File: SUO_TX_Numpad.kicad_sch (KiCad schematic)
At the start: 17 parts, among them J1 USB_C_Receptacle_USB2.0_16P, SW1 BOOT, U1 STM32F411CEUx, U2 XC6206PxxxMR-Regulator_Linear, U3 USBLC6-2SC6, Y1 XTAL OSC XO 8.0000MHZ HCMOS S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

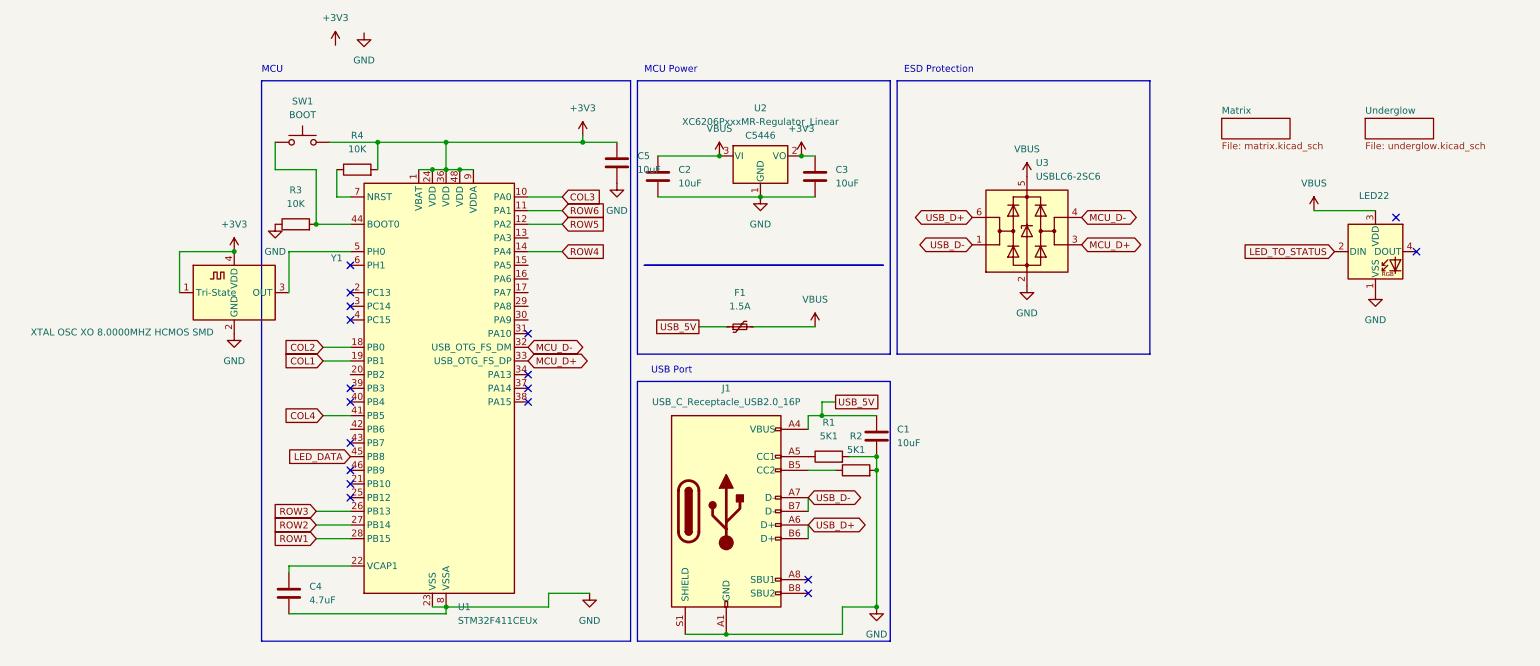
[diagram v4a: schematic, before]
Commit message: Pulled A10 to ground; found that a BlackPill dev board wo'nt DFU properly without it. Updated SK6812MINI-E footprint to be a rotated one; track layout stays the same, but the old footprint was incorrect, resulting in all key LEDs shorting out
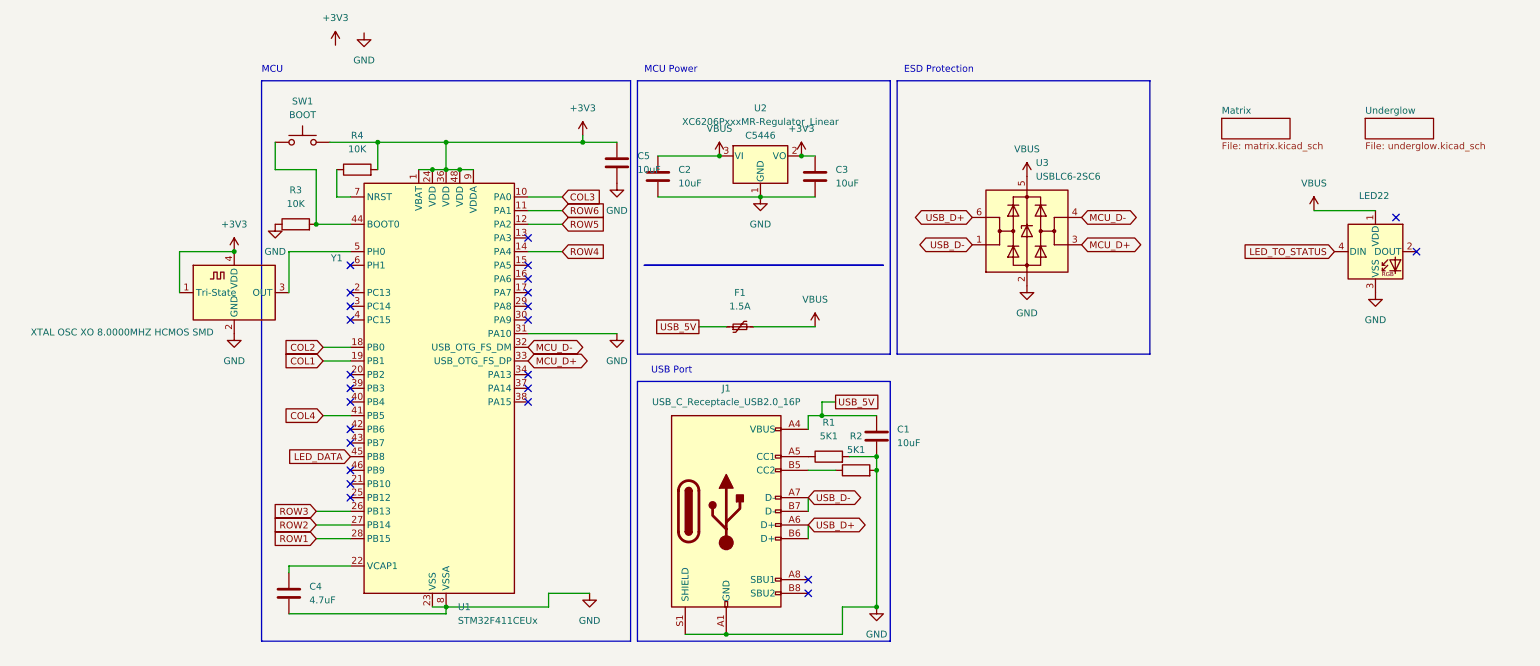
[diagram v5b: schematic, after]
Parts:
- LED22: footprint kicad-keyboard-parts:MX_SK6812MINI-E_REV -> kicad-keyboard-parts:MX_SK6812MINI-E_REV_ROTATED; symbol LED:SK6812MINI-E -> kicad-keyboard-parts:SK6812MINI-E
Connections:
- net GND: now also LED22.3 (VSS), U1.31 (PA10); no longer LED22.1 (VSS)
- net LED_TO_STATUS: now also LED22.4 (DIN); no longer LED22.2 (DIN)
- net VBUS: now also LED22.1 (VDD); no longer LED22.3 (VDD)
- no-connect marks 18 -> 25
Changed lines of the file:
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@@
 	)
 	(no_connect
-		(at 78.74 72.39)
-	)
-	(no_connect
 		(at 45.72 100.33)
 	)
@@
 	)
 	(no_connect
+		(at 78.74 67.31)
+	)
+	(no_connect
 		(at 45.72 82.55)
 	)
@@
 	)
 	(no_connect
+		(at 78.74 59.69)
+	)
+	(no_connect
+		(at 45.72 90.17)
+	)
+	(no_connect
 		(at 45.72 67.31)
 	)
@@
 	)
 	(no_connect
+		(at 78.74 69.85)
+	)
+	(no_connect
 		(at 130.81 118.11)
 	)
 	(no_connect
+		(at 45.72 80.01)
+	)
+	(no_connect
+		(at 78.74 62.23)
+	)
+	(no_connect
 		(at 78.74 82.55)
 	)
 	(no_connect
+		(at 78.74 64.77)
+	)
+	(no_connect
+		(at 78.74 54.61)
+	)
+	(no_connect
 		(at 45.72 85.09)
 	)
@@
 	(wire
 		(pts
+			(xy 78.74 72.39) (xy 95.25 72.39)
+		)
+		(stroke
+			(width 0)
+			(type default)
+		)
+	)
+	(wire
+		(pts
 			(xy 130.81 107.95) (xy 130.81 110.49)
 		)
@@
 	)
 	(symbol
-		(lib_id "LED:SK6812MINI-E")
+		(lib_id "kicad-keyboard-parts:SK6812MINI-E")
 		(at 236.22 57.15 0)
 		(unit 1)
@@
 			)
 		)
-		(property "Footprint" "kicad-keyboard-parts:MX_SK6812MINI-E_REV"
+		(property "Footprint" "kicad-keyboard-parts:MX_SK6812MINI-E_REV_ROTATED"
 			(at 237.49 64.77 0)
 			(effects
@@
 					(unit 1)
 				)
+			)
+		)
+	)
+	(symbol
+		(lib_id "power:GND")
+		(at 95.25 72.39 0)
+		(unit 1)
+		(exclude_from_sim no)
+		(in_bom yes)
+		(on_board yes)
+		(dnp no)
+		(fields_autoplaced yes)
+		(property "Reference" "#PWR037"
+			(at 95.25 78.74 0)
+			(effects
+				(font
+					(size 1.27 1.27)
+				)
+				(hide yes)
+			)
+		)
+		(property "Value" "GND"
+			(at 95.25 77.47 0)
+			(effects
+				(font
+					(size 1.27 1.27)
+				)
+			)
+		)
+		(property "Footprint" ""
+			(at 95.25 72.39 0)
+			(effects
+				(font
+					(size 1.27 1.27)
+				)
+				(hide yes)
+			)
+		)
+		(property "Datasheet" ""
+			(at 95.25 72.39 0)
+			(effects
+				(font
+					(size 1.27 1.27)
+				)
+				(hide yes)
+			)
+		)
+		(property "Description" ""
+			(at 95.25 72.39 0)
+			(effects
+				(font
+					(size 1.27 1.27)
+				)
+			)
+		)
+		(pin "1"
+		)
+		(instances
+			(project "SUO_TX_Numpad"
+				(path "/4f42914a-d4c6-4461-b1c3-be7726ab46dc"
+					(reference "#PWR037")
+					(unit 1)
+				)

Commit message: Added 3225 active oscillator, unsure if pin 1 is in fact enable, is in fact active high, so a jumper pad to pick either is added
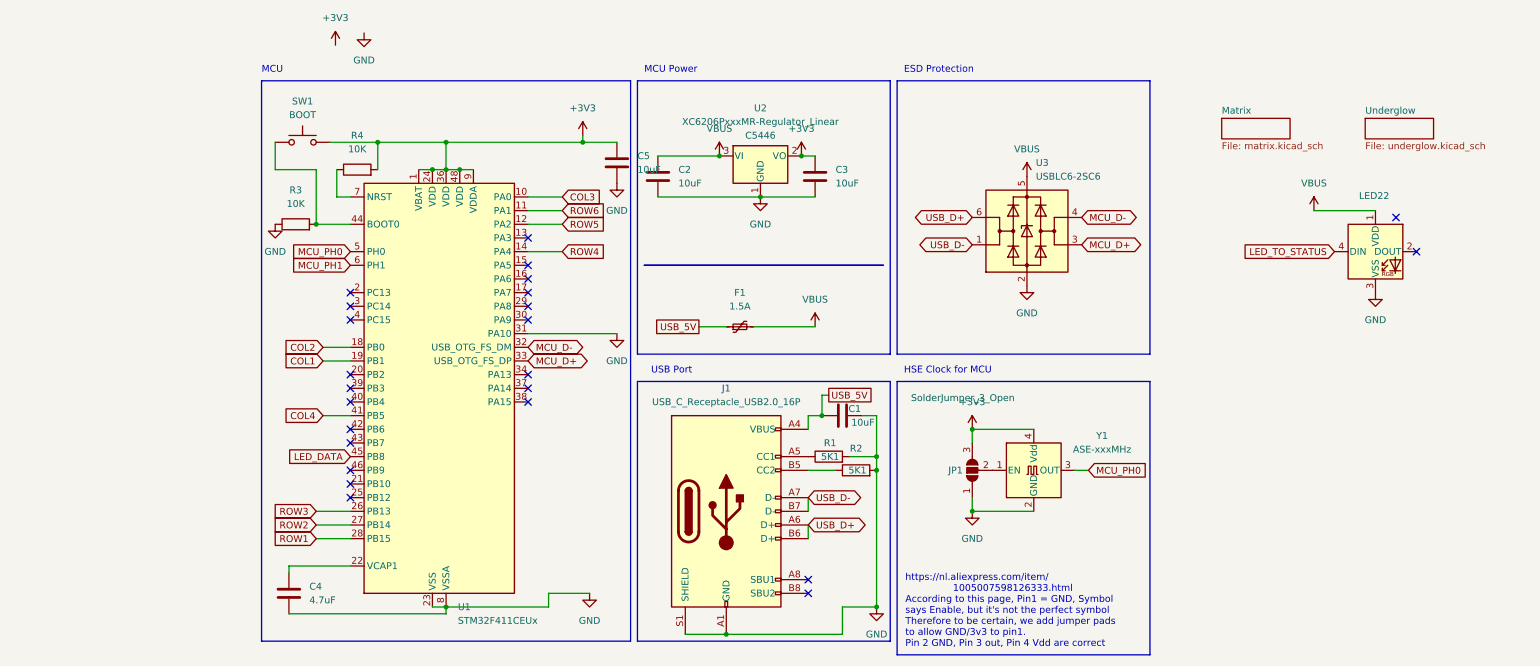
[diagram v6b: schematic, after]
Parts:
- removed Y1: XTAL OSC XO 8.0000MHZ HCMOS SMD, Oscillator:Oscillator_SMD_ECS_2520MV-xxx-xx-4Pin_2.5x2.0mm, symbol Oscillator:ECS-2520MV-xxx-xx
- added JP1: SolderJumper_3_Open, Jumper:SolderJumper-3_P1.3mm_Open_RoundedPad1.0x1.5mm, symbol Jumper:SolderJumper_3_Open
- added Y1: ASE-xxxMHz, Oscillator:Oscillator_SMD_Abracon_ASE-4Pin_3.2x2.5mm, symbol Oscillator:ASE-xxxMHz
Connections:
- net +3V3: now also JP1.3 (B), Y1.4 (Vdd)
- net GND: now also JP1.1 (A), Y1.2 (GND)
- net MCU_PH0: now reaches U1.5 (PH0)
- net MCU_PH0: now also Y1.3 (OUT)
- net MCU_PH1: now reaches U1.6 (PH1)
- new net: JP1.2 (C), Y1.1 (EN)
- no-connect marks 25 -> 24
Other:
- note added: "HSE Clock for MCU"
- note added: "https://nl.aliexpress.com/item/ 1005007598126333.html According to this page, Pin1 = GND, Symbol says Enable, but it's not the perfect symbol Therefore to be certain, we add jumper pads to allow GND/3v3 to pin1. Pin 2 GND, Pin 3 out, Pin 4 Vdd are correct"
- moved on the sheet: C1

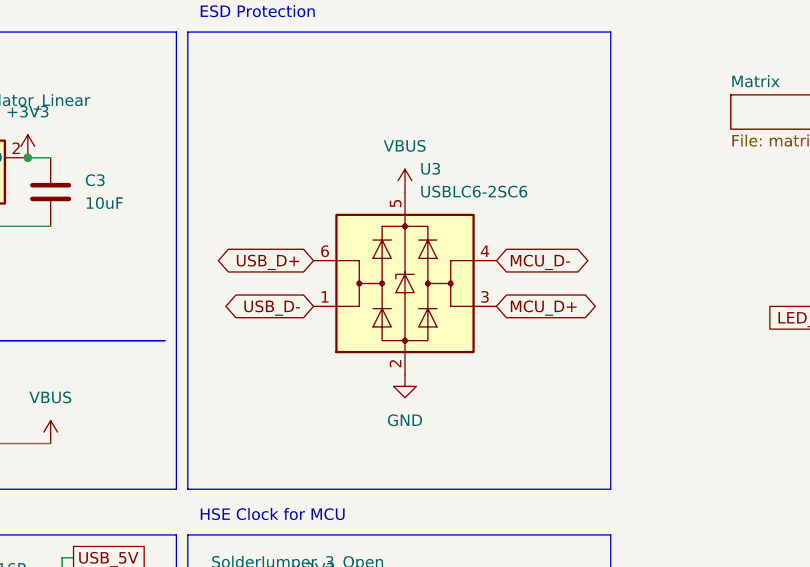
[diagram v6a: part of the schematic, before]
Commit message: Fixed wiring mistake on USBLC6-2SC6
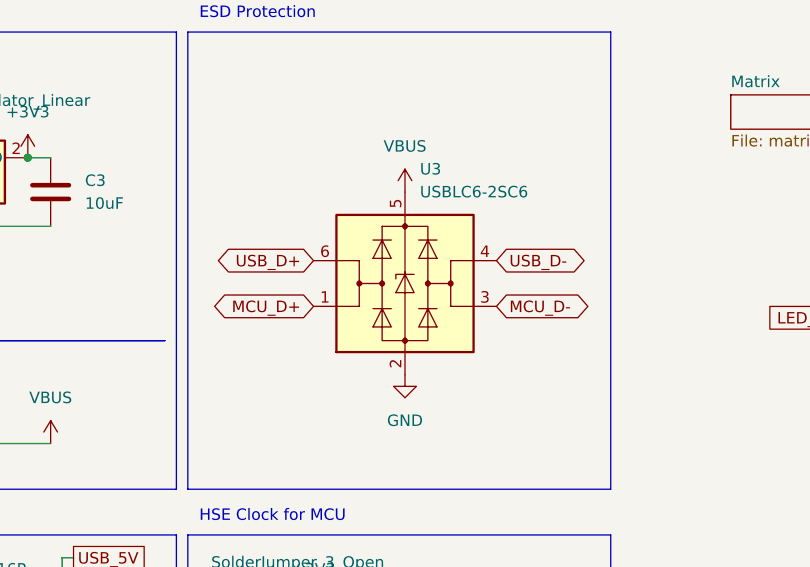
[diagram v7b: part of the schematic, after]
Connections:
- net MCU_D+: now also U3.1 (I/O1); no longer U3.3 (I/O2)
- net MCU_D-: now also U3.3 (I/O2); no longer U3.4 (I/O2)
- net USB_D-: now also U3.4 (I/O2); no longer U3.1 (I/O1)
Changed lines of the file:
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@@
+		)
+	)
+	(global_label "ROW4"
+		(shape input)
+		(at 85.09 57.15 0)
+		(fields_autoplaced yes)
+		(effects
+			(font
+				(size 1.27 1.27)
+			)
+			(justify left)
+		)
+		(property "Intersheetrefs" "${INTERSHEET_REFS}"
+			(at 93.3366 57.15 0)
+			(effects
+				(font
+					(size 1.27 1.27)
+				)
+				(justify left)
+				(hide yes)
+			)
+		)
+	)
+	(global_label "COL1"
+		(shape input)
+		(at 40.64 77.47 180)
+		(fields_autoplaced yes)
+		(effects
+			(font
+				(size 1.27 1.27)
+			)
+			(justify right)
+		)
+		(property "Intersheetrefs" "${INTERSHEET_REFS}"
+			(at 32.8167 77.47 0)
+			(effects
+				(font
+					(size 1.27 1.27)
+				)
+				(justify right)
+				(hide yes)
+			)
+		)
+	)
+	(global_label "USB_D-"
+		(shape bidirectional)
+		(at 130.81 102.87 0)
+		(fields_autoplaced yes)
+		(effects
+			(font
+				(size 1.27 1.27)
+			)
+			(justify left)
+		)
+		(property "Intersheetrefs" "${INTERSHEET_REFS}"
+			(at 142.5265 102.87 0)
+			(effects
+				(font
+					(size 1.27 1.27)
+				)
+				(justify left)
+				(hide yes)
+			)
 		)
 	)
 	(global_label "MCU_D-"
 		(shape bidirectional)
-		(at 181.61 50.8 0)
-		(fields_autoplaced yes)
-		(effects
-			(font
-				(size 1.27 1.27)
-			)
-			(justify left)
-		)
-		(property "Intersheetrefs" "${INTERSHEET_REFS}"
-			(at 193.5684 50.8 0)
-			(effects
-				(font
-					(size 1.27 1.27)
-				)
-				(justify left)
+		(at 181.61 55.88 0)
+		(fields_autoplaced yes)
+		(effects
+			(font
+				(size 1.27 1.27)
+			)
+			(justify left)
+		)
+		(property "Intersheetrefs" "${INTERSHEET_REFS}"
+			(at 193.5684 55.88 0)
+			(effects
+				(font
+					(size 1.27 1.27)
+				)
+				(justify left)
+				(hide yes)
+			)
+		)
+	)
+	(global_label "MCU_PH0"
+		(shape input)
+		(at 45.72 57.15 180)
+		(fields_autoplaced yes)
+		(effects
+			(font
+				(size 1.27 1.27)
+			)
+			(justify right)
+		)
+		(property "Intersheetrefs" "${INTERSHEET_REFS}"
+			(at 33.9053 57.15 0)
+			(effects
+				(font
+					(size 1.27 1.27)
+				)
+				(justify right)
+				(hide yes)
+			)
+		)
+	)
+	(global_label "ROW3"
+		(shape input)
+		(at 39.37 105.41 180)
+		(fields_autoplaced yes)
+		(effects
+			(font
+				(size 1.27 1.27)
+			)
+			(justify right)
+		)
+		(property "Intersheetrefs" "${INTERSHEET_REFS}"
+			(at 31.1234 105.41 0)
+			(effects
+				(font
+					(size 1.27 1.27)
+				)
+				(justify right)
+				(hide yes)
+			)
+		)
+	)
+	(global_label "MCU_PH1"
+		(shape input)
+		(at 45.72 59.69 180)
+		(fields_autoplaced yes)
+		(effects
+			(font
+				(size 1.27 1.27)
+			)
+			(justify right)
+		)
+		(property "Intersheetrefs" "${INTERSHEET_REFS}"
+			(at 33.9053 59.69 0)
+			(effects
+				(font
+					(size 1.27 1.27)
+				)
+				(justify right)
 				(hide yes)
 			)
@@
 		)
 	)
-	(global_label "ROW4"
-		(shape input)
-		(at 85.09 57.15 0)
-		(fields_autoplaced yes)
-		(effects
-			(font
-				(size 1.27 1.27)
-			)
-			(justify left)
-		)
-		(property "Intersheetrefs" "${INTERSHEET_REFS}"
-			(at 93.3366 57.15 0)
-			(effects
-				(font
-					(size 1.27 1.27)
-				)
-				(justify left)
-				(hide yes)
-			)
-		)
-	)
-	(global_label "COL1"
-		(shape input)
-		(at 40.64 77.47 180)
-		(fields_autoplaced yes)
-		(effects
-			(font
-				(size 1.27 1.27)
-			)
-			(justify right)
-		)
-		(property "Intersheetrefs" "${INTERSHEET_REFS}"
-			(at 32.8167 77.47 0)
-			(effects
-				(font
-					(size 1.27 1.27)
-				)
-				(justify right)
-				(hide yes)
-			)
-		)
-	)
-	(global_label "USB_D-"
-		(shape bidirectional)
-		(at 130.81 102.87 0)
-		(fields_autoplaced yes)
-		(effects
-			(font
-				(size 1.27 1.27)
-			)
-			(justify left)
-		)
-		(property "Intersheetrefs" "${INTERSHEET_REFS}"
-			(at 142.5265 102.87 0)
-			(effects
-				(font
-					(size 1.27 1.27)
-				)
-				(justify left)
-				(hide yes)
-			)
-		)
-	)
-	(global_label "USB_D-"
+	(global_label "ROW2"
+		(shape input)
+		(at 39.37 107.95 180)
+		(fields_autoplaced yes)
+		(effects
+			(font
+				(size 1.27 1.27)
+			)
+			(justify right)
+		)
+		(property "Intersheetrefs" "${INTERSHEET_REFS}"
+			(at 31.1234 107.95 0)
+			(effects
+				(font
+					(size 1.27 1.27)
+				)
+				(justify right)
+				(hide yes)
+			)
+		)
+	)
+	(global_label "MCU_D+"
 		(shape bidirectional)
 		(at 161.29 55.88 180)
@@
 		)
 		(property "Intersheetrefs" "${INTERSHEET_REFS}"
-			(at 149.5735 55.88 0)
-			(effects
-				(font
-					(size 1.27 1.27)
-				)
-				(justify right)
-				(hide yes)
-			)
-		)
-	)
-	(global_label "MCU_PH0"
-		(shape input)
-		(at 45.72 57.15 180)
-		(fields_autoplaced yes)
-		(effects
-			(font
-				(size 1.27 1.27)
-			)
-			(justify right)
-		)
-		(property "Intersheetrefs" "${INTERSHEET_REFS}"
-			(at 33.9053 57.15 0)
-			(effects
-				(font
-					(size 1.27 1.27)
-				)
-				(justify right)
-				(hide yes)
-			)
-		)
-	)
-	(global_label "ROW3"
-		(shape input)
-		(at 39.37 105.41 180)
-		(fields_autoplaced yes)
-		(effects
-			(font
-				(size 1.27 1.27)
-			)
-			(justify right)
-		)
-		(property "Intersheetrefs" "${INTERSHEET_REFS}"
-			(at 31.1234 105.41 0)
-			(effects
-				(font
-					(size 1.27 1.27)
-				)
-				(justify right)
-				(hide yes)
-			)
-		)
-	)
-	(global_label "MCU_PH1"
-		(shape input)
-		(at 45.72 59.69 180)
-		(fields_autoplaced yes)
-		(effects
-			(font
-				(size 1.27 1.27)
-			)
-			(justify right)
-		)
-		(property "Intersheetrefs" "${INTERSHEET_REFS}"
-			(at 33.9053 59.69 0)
-			(effects
-				(font
-					(size 1.27 1.27)
-				)
-				(justify right)
-				(hide yes)
-			)
-		)
-	)
-	(global_label "ROW2"
-		(shape input)
-		(at 39.37 107.95 180)
-		(fields_autoplaced yes)
-		(effects
-			(font
-				(size 1.27 1.27)
-			)
-			(justify right)
-		)
-		(property "Intersheetrefs" "${INTERSHEET_REFS}"
-			(at 31.1234 107.95 0)
+			(at 149.3316 55.88 0)
 			(effects
 				(font
@@
 		)
 	)
-	(global_label "MCU_D+"
-		(shape bidirectional)
-		(at 181.61 55.88 0)
-		(fields_autoplaced yes)
-		(effects
-			(font
-				(size 1.27 1.27)
-			)
-			(justify left)
-		)
-		(property "Intersheetrefs" "${INTERSHEET_REFS}"
-			(at 193.5684 55.88 0)
-			(effects
-				(font
+	(global_label "USB_D-"
+		(shape bidirectional)
+		(at 181.61 50.8 0)
+		(fields_autoplaced yes)
+		(effects
+			(font
+				(size 1.27 1.27)
+			)
+			(justify left)
+		)
+		(property "Intersheetrefs" "${INTERSHEET_REFS}"
+			(at 193.3265 50.8 0)
+			(effects
+				(font
